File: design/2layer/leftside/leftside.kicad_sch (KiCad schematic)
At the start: 227 parts, among them IC2 MCP23009-E_MG, IC3 nRF52833-QDAA-R7, IC5 XCL110A503KR-G, IC6 TPS22917LDBVT, IC7 SN74AHCT1G125DCKR, IC8 TPS63051RMWT, J1 USB_C_Receptacle_USB2.0_16P, J2 Battery+, J3 Battery-, J4 OLED_128x32, J5 Conn_01x01, J6 Conn_01x04, J7 F32Q-1A7H1-11012, J8 Conn_01x01, U1 BQ27441-G1, U2 BQ24072RGT, U3 USB6B1, U5 PEC11L-4015F-S0015, Y1 ECS-320-8-37B2-JTY-TR

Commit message: Left side pre-stich
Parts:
- removed 3v3_1: TestPoint, TestPoint:TestPoint_Pad_D1.5mm, symbol Connector:TestPoint
- removed Di31, Di32, Di33, Di35: Diode, ScottoKeebs_Components:Diode_SOD-123, symbol ScottoKeebs:Placeholder_Diode
- removed S14, S24, S32, S33, S34, S36, S8: Keyswitch, ScottoKeebs_Hotswap:Hotswap_Choc_V1V2_Plated_1.00u, symbol ScottoKeebs:Placeholder_Keyswitch
- added C2, C3, C4: 100nF, ScottoKeebs_Components:Capacitor_0603, symbol Device:C_Small
- added D49, D50, D51, D52, D53, D54, D55, D56, D57, D58, D59, D60, D61, D62, D63: LED_SK6812MINI, ScottoKeebs_Components:LED_SK6812MINI, symbol ScottoKeebs:LED_SK6812MINI
- added PC3: 10uF, ScottoKeebs_Components:Capacitor_0603, symbol Device:C_Small
- added S3, S4, S5: Keyswitch, ScottoKeebs_Hotswap:Hotswap_Choc_V1V2_Plated_1.00u, symbol ScottoKeebs:Placeholder_Keyswitch
- J2, J3: footprint Connector_Wire:SolderWire-2.5sqmm_1x01_D2.4mm_OD3.6mm -> Connector_Wire:SolderWire-0.75sqmm_1x01_D1.25mm_OD2.3mm
- J5, J8: footprint (none) -> TestPoint:TestPoint_Pad_1.0x1.0mm
- PG1, VBUS_1, VBUS_USB1: footprint TestPoint:TestPoint_Pad_D1.5mm -> TestPoint:TestPoint_Pad_D1.0mm
- renumbered S25 to S0, S27 to S10, S9 to S11, S10 to S12, S11 to S13, S12 to S14, S28 to S15, S15 to S16, S16 to S17, S17 to S18, S18 to S19, S29 to S20, S20 to S21, S21 to S22, S22 to S23, S23 to S24, S30 to S25, S7 to S26, S13 to S27, S19 to S28, S26 to S29, S31 to S30, S35 to S33, S37 to S35, S3 to S6, S4 to S7, S5 to S8, S6 to S9, R10 to SR10
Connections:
- net 5V: now also C2.1, C3.1, C4.1, D49.1 (VDD), D50.1 (VDD), D51.1 (VDD), D52.1 (VDD), D53.1 (VDD), D54.1 (VDD), D55.1 (VDD), D56.1 (VDD), D57.1 (VDD), D58.1 (VDD), D59.1 (VDD), D60.1 (VDD), D61.1 (VDD), D62.1 (VDD), D63.1 (VDD)
- net CCW: now also IC3.14 (P0.15); no longer IC3.15 (P0.17)
- net CHG: now also IC3.6 (P1.09); no longer IC3.4 (P0.04)
- net CW: now also IC3.15 (P0.17); no longer IC3.14 (P0.15)
- net Column 0: now also IC3.33 (P0.28), S11.1, S16.1, S21.1, S26.1, S6.1; no longer IC3.36 (P0.31), S2.1
- net Column 1: now also S12.1, S17.1, S2.1, S22.1, S27.1, S7.1; no longer S11.1, S16.1, S21.1, S26.1, S6.1
- net Column 2: now also IC3.17 (P0.20), S13.1, S18.1, S23.1, S28.1, S33.1, S8.1, S3.1; no longer IC3.34 (P0.29), S12.1, S17.1, S22.1, S27.1, S7.1
- net Column 3: now also IC3.34 (P0.29), S14.1, S19.1, S24.1, S29.1, S9.1, S4.1; no longer IC3.33 (P0.28), S13.1, S18.1, S23.1, S28.1, S33.1, S8.1
- net Column 4: now also IC3.36 (P0.31), S10.1, S15.1, S20.1, S25.1, S30.1, S35.1, S5.1; no longer IC3.32 (P0.02), S14.1, S19.1, S24.1, S29.1, S9.1
- net GND: now also C2.2, C3.2, C4.2, D49.3 (VSS), D50.3 (VSS), D51.3 (VSS), D52.3 (VSS), D53.3 (VSS), D54.3 (VSS), D55.3 (VSS), D56.3 (VSS), D57.3 (VSS), D58.3 (VSS), D59.3 (VSS), D60.3 (VSS), D61.3 (VSS), D62.3 (VSS), D63.3 (VSS), PC3.2
- net GPOUT: now also IC3.4 (P0.04); no longer IC3.5 (P0.05)
- net INTA: now also IC3.32 (P0.02); no longer IC3.23 (P0.10)
- net LED: now also IC3.31 (P0.03); no longer IC3.17 (P0.20)
- net NO: now also IC3.7 (P0.11); no longer IC3.6 (P1.09)
- net NO2: now also IC3.5 (P0.05); no longer IC3.7 (P0.11)
- net Row 0: now also Di1.1 (K), Di12.1 (K), Di16.1 (K), Di24.1 (K), IC2.12 (GP3); no longer Di10.1 (K), Di2.1 (K), Di26.1 (K), Di8.1 (K), Di9.1 (K), IC2.9 (GP0)
- net Row 1: now also Di10.1 (K), Di2.1 (K), Di26.1 (K), Di8.1 (K), Di9.1 (K), IC2.13 (GP4); no longer Di12.1 (K), Di13.1 (K), Di14.1 (K), Di15.1 (K), Di27.1 (K), Di3.1 (K), IC2.10 (GP1)
- net Row 2: now also Di13.1 (K), Di14.1 (K), Di15.1 (K), Di27.1 (K), Di3.1 (K), IC2.14 (GP5); no longer Di16.1 (K), Di17.1 (K), Di18.1 (K), Di19.1 (K), Di28.1 (K), Di5.1 (K), IC2.11 (GP2)
- net Row 3: now also Di18.1 (K), Di19.1 (K), Di28.1 (K), Di5.1 (K), IC2.15 (GP6); no longer Di22.1 (K), Di23.1 (K), Di24.1 (K), Di29.1 (K), Di6.1 (K), IC2.12 (GP3)
- net Row 4: now also Di17.1 (K), Di22.1 (K), Di23.1 (K), Di29.1 (K), Di6.1 (K), IC2.16 (GP7); no longer Di1.1 (K), Di11.1 (K), Di20.1 (K), Di25.1 (K), Di30.1 (K), Di4.1 (K), IC2.13 (GP4)
- net Row 5: now also Di11.1 (K), Di20.1 (K), Di25.1 (K), Di30.1 (K), Di4.1 (K), IC2.10 (GP1); no longer Di34.1 (K), Di36.1 (K), IC2.14 (GP5)
- net at D6.2 (DOUT): now also D5.4 (DIN); no longer D7.4 (DIN)
- net at D6.4 (DIN): now also D7.2 (DOUT); no longer D5.2 (DOUT)
- net at D17.2 (DOUT): now also D16.4 (DIN); no longer D18.4 (DIN)
- net at D17.4 (DIN): now also D18.2 (DOUT); no longer D16.2 (DOUT)
- net at D3.2 (DOUT): now also D2.4 (DIN); no longer D4.4 (DIN)
- net at D3.4 (DIN): now also D4.2 (DOUT); no longer D2.2 (DOUT)
- net at D28.2 (DOUT): now also D27.4 (DIN); no longer D29.4 (DIN)
- net at D28.4 (DIN): now also D29.2 (DOUT); no longer D27.2 (DOUT)
- net at IC5.1 (1/VIN), IC5.3 (3/EN), IC5.7 (7/L1)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: now also PC3.1
- net at D30.4 (DIN): now also D53.2 (DOUT); no longer D29.2 (DOUT)
- net at D15.2 (DOUT): now also D14.4 (DIN); no longer D16.4 (DIN)
- net at D15.4 (DIN): now also D16.2 (DOUT); no longer D14.2 (DOUT)
- net at D41.2 (DOUT): now also D40.4 (DIN); no longer D42.4 (DIN)
- net at D41.4 (DIN): now also D42.2 (DOUT); no longer D40.2 (DOUT)
- net at D37.2 (DOUT): now also D36.4 (DIN); no longer D38.4 (DIN)
- net at D37.4 (DIN): now also D38.2 (DOUT); no longer D36.2 (DOUT)
- net at D45.2 (DOUT): now also D44.4 (DIN); no longer D46.4 (DIN)
- net at D45.4 (DIN): now also D46.2 (DOUT); no longer D44.2 (DOUT)
- net at D30.2 (DOUT): now also D29.4 (DIN); no longer D31.4 (DIN)
- net at D21.2 (DOUT): now also D20.4 (DIN); no longer D22.4 (DIN)
- net at D21.4 (DIN): now also D22.2 (DOUT); no longer D20.2 (DOUT)
- net at Di16.2 (A): now also S4.2
- net at D35.2 (DOUT): now also D34.4 (DIN); no longer D36.4 (DIN)
- net at D35.4 (DIN): now also D36.2 (DOUT); no longer D34.2 (DOUT)
- net at D33.2 (DOUT): now also D32.4 (DIN); no longer D34.4 (DIN)
- net at D39.4 (DIN): now also D40.2 (DOUT); no longer D38.2 (DOUT)
- net at D47.4 (DIN): now also D26.2 (DOUT); no longer D46.2 (DOUT)
- net at D25.2 (DOUT): now also D24.4 (DIN); no longer D26.4 (DIN)
- net at D25.4 (DIN): now also D23.2 (DOUT); no longer D24.2 (DOUT)
- net at D39.2 (DOUT): now also D38.4 (DIN); no longer D40.4 (DIN)
- net at D19.2 (DOUT): now also D52.4 (DIN); no longer D20.4 (DIN)
- net at Di12.2 (A): now also S3.2
- net at D13.2 (DOUT): now also D12.4 (DIN); no longer D14.4 (DIN)
- net at D13.4 (DIN): now also D14.2 (DOUT); no longer D12.2 (DOUT)
- net at D19.4 (DIN): now also D20.2 (DOUT); no longer D18.2 (DOUT)
- net at D1.2 (DOUT): no longer D2.4 (DIN)
- net at SR10.2: now also D49.4 (DIN); no longer D1.4 (DIN)
- net at D48.2 (DOUT): now also D4.4 (DIN)
- net at D48.4 (DIN): now also D5.2 (DOUT); no longer D47.2 (DOUT)
- net at D43.4 (DIN): now also D44.2 (DOUT); no longer D42.2 (DOUT)
- net at Di24.2 (A): now also S5.2
- net at D8.2 (DOUT): now also D10.4 (DIN); no longer D9.4 (DIN)
- net at D8.4 (DIN): now also D9.2 (DOUT); no longer D7.2 (DOUT)
- net at D33.4 (DIN): now also D34.2 (DOUT); no longer D32.2 (DOUT)
- net at D31.2 (DOUT): now also D54.4 (DIN); no longer D32.4 (DIN)
- net at D23.4 (DIN): now also D47.2 (DOUT); no longer D22.2 (DOUT)
- net at Di17.2 (A): now also S21.2; no longer S16.2
- net at Di21.2 (A): now also S16.2; no longer S21.2
- net at D43.2 (DOUT): now also D56.4 (DIN); no longer D44.4 (DIN)
- net at D11.2 (DOUT): now also D7.4 (DIN); no longer D12.4 (DIN)
- net at D10.2 (DOUT): now also D46.4 (DIN); no longer D11.4 (DIN)
- removed net Column 5: IC3.31 (P0.03), S10.1, S15.1, S20.1, S25.1, S30.1, S35.1
- new net: D58.2 (DOUT), D60.4 (DIN)
- new net: D57.2 (DOUT), D58.4 (DIN)
- new net: D18.4 (DIN), D51.2 (DOUT)
- new net: D51.4 (DIN), D52.2 (DOUT)
- new net: D59.4 (DIN), D60.2 (DOUT)
- new net: D62.4 (DIN), D63.2 (DOUT)
- new net: D59.2 (DOUT), D63.4 (DIN)
- new net: D53.4 (DIN), D54.2 (DOUT)
- new net: D42.4 (DIN), D55.2 (DOUT)
- new net: D55.4 (DIN), D56.2 (DOUT)
- new net: D22.4 (DIN), D24.2 (DOUT)
- new net: D49.2 (DOUT), D50.4 (DIN)
- new net: D1.4 (DIN), D2.2 (DOUT)
- new net: D31.4 (DIN), D32.2 (DOUT)
- new net: D61.4 (DIN), D62.2 (DOUT)
- new net: D61.2 (DOUT), D9.4 (DIN)
- new net: D50.2 (DOUT), D57.4 (DIN)
- new net: D11.4 (DIN), D12.2 (DOUT)
- new net: D26.4 (DIN), D27.2 (DOUT)
- new net Row 6: Di34.1 (K), Di36.1 (K), IC2.11 (GP2)
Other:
- moved on the sheet: C21, C28, C29, C30, C31, C32, C33, C34, C35, C36, C38, C39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

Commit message: LS Kicad 10 migration
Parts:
- removed VBUS_USB1: TestPoint, TestPoint:TestPoint_Pad_D1.0mm, symbol Connector:TestPoint
- EVQWGD1: value ~ -> (none)
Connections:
- net GND: now also J1.SH (SHIELD); no longer J1.S1 (SHIELD)
- net at D49.4 (DIN): now also SR10.1; no longer SR10.2
- net at IC7.4 (Y): now also SR10.2; no longer SR10.1
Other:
- moved on the sheet: 3V3_2, 5V_1, 5V_4, C2, C21, C28, C29, C3, C30, C31, C32, C33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

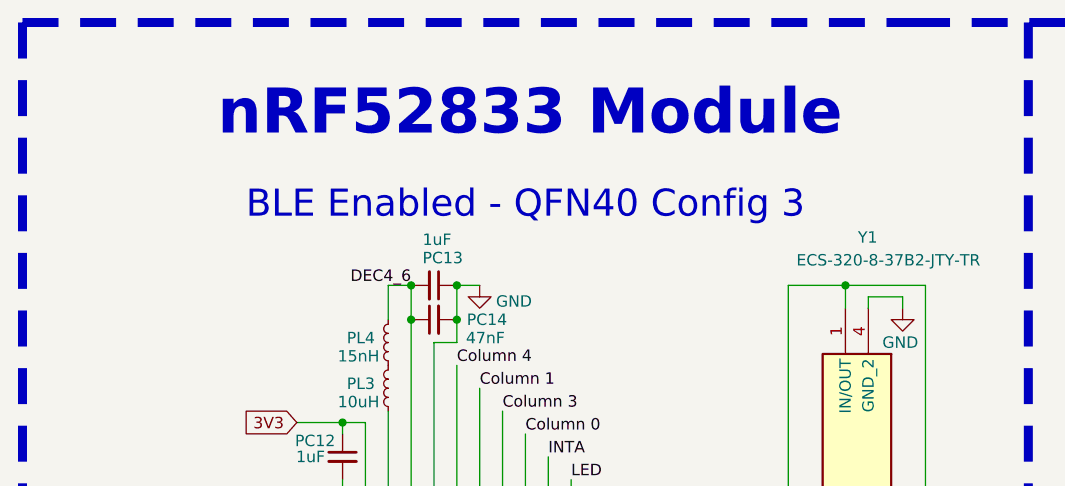
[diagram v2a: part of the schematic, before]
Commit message: RS LED wiring
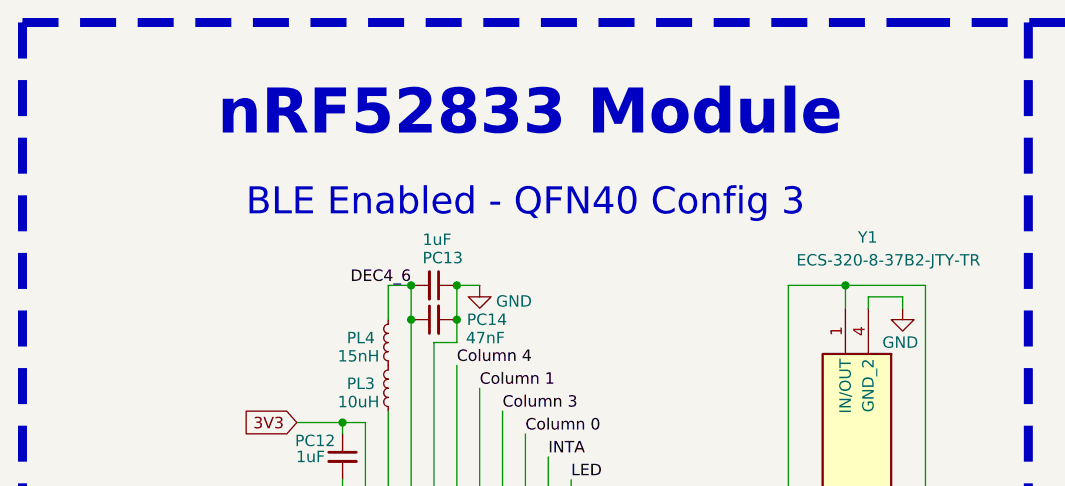
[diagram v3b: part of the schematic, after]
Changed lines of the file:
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@@
 	(text "BLE Enabled - QFN40 Config 3\n"
 		(exclude_from_sim no)
-		(at 69.85 34.29 0)
+		(at 69.85 34.036 0)
 		(effects
 			(font

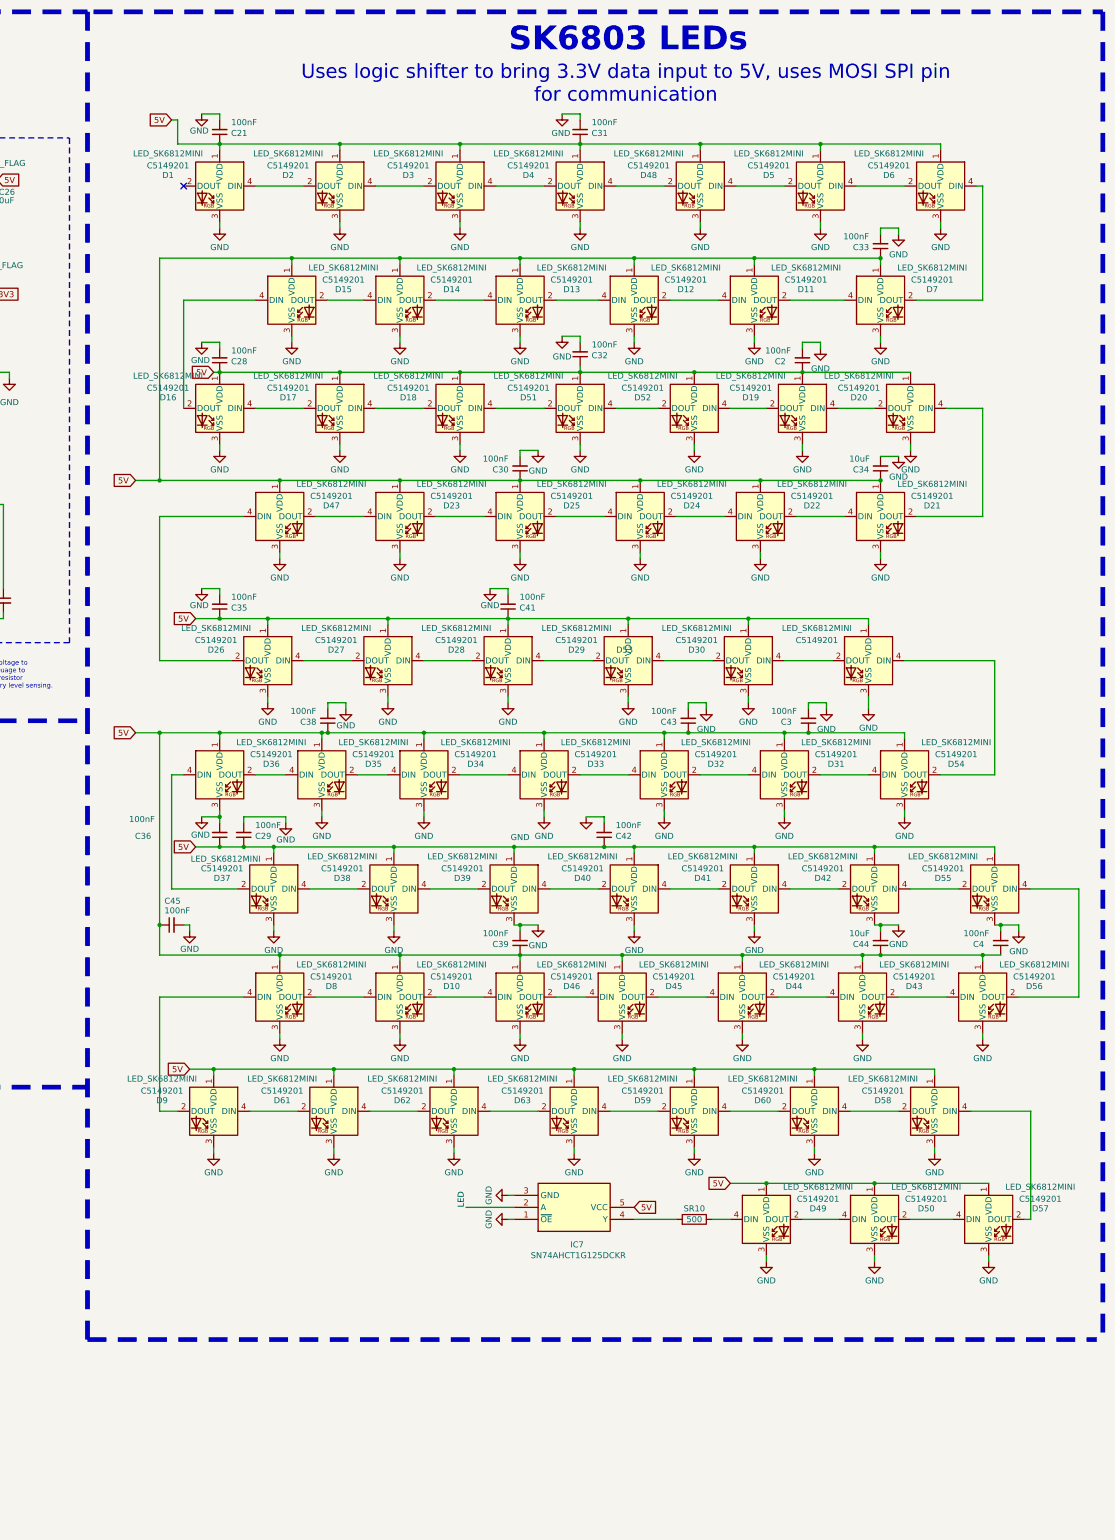
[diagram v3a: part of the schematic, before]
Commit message: Commit before changing via sizes
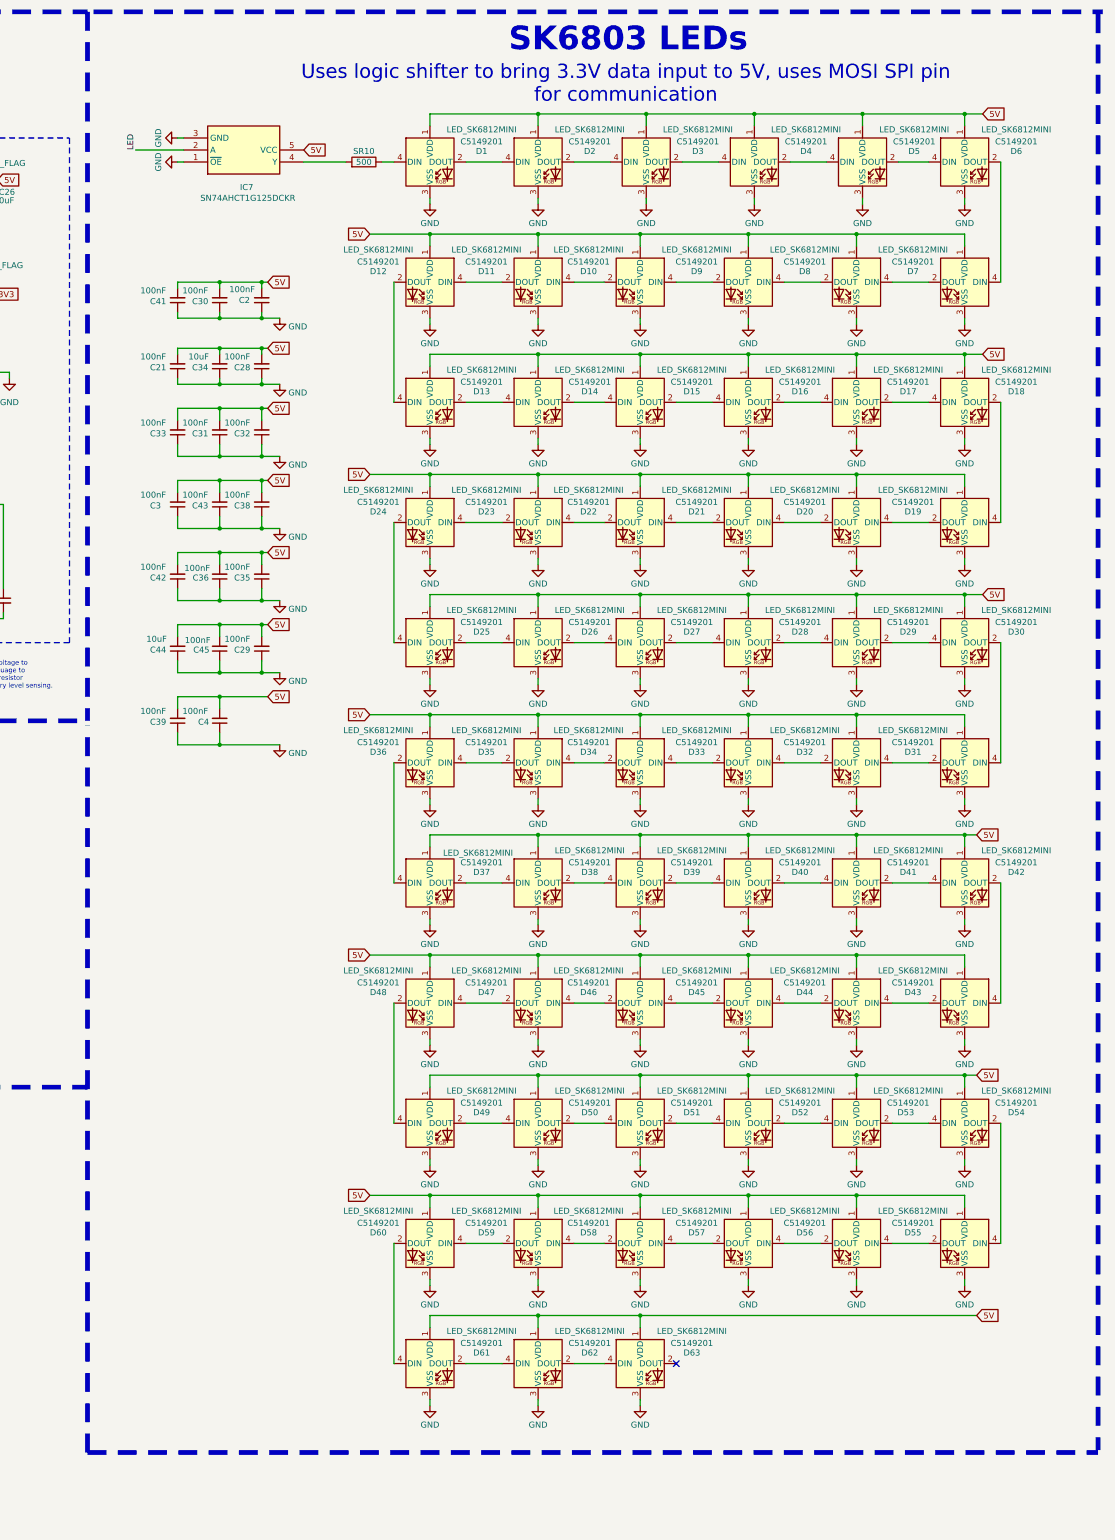
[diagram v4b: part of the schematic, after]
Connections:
- net 5V: now also C2.2, C21.2, C28.2, C29.2, C3.2, C30.2, C31.2, C32.2, C33.2, C34.2, C35.2, C36.2, C38.2, C39.2, C4.2, C41.2, C42.2, C43.2, C44.2, C45.2; no longer C2.1, C21.1, C28.1, C29.1, C3.1, C30.1, C31.1, C32.1, C33.1, C34.1, C35.1, C36.1, C38.1, C39.1, C4.1, C41.1, C42.1, C43.1, C44.1, C45.1
- net GND: now also C2.1, C21.1, C28.1, C29.1, C3.1, C30.1, C31.1, C32.1, C33.1, C34.1, C35.1, C36.1, C38.1, C39.1, C4.1, C41.1, C42.1, C43.1, C44.1, C45.1; no longer C2.2, C21.2, C28.2, C29.2, C3.2, C30.2, C31.2, C32.2, C33.2, C34.2, C35.2, C36.2, C38.2, C39.2, C4.2, C41.2, C42.2, C43.2, C44.2, C45.2
- net at D60.4 (DIN): now also D59.2 (DOUT); no longer D58.2 (DOUT)
- net at D17.2 (DOUT): now also D18.4 (DIN); no longer D16.4 (DIN)
- net at D17.4 (DIN): now also D16.2 (DOUT); no longer D18.2 (DOUT)
- net at D2.4 (DIN): now also D1.2 (DOUT); no longer D3.2 (DOUT)
- net at D3.4 (DIN): now also D2.2 (DOUT); no longer D4.2 (DOUT)
- net at D5.4 (DIN): now also D4.2 (DOUT); no longer D6.2 (DOUT)
- net at D6.4 (DIN): now also D5.2 (DOUT); no longer D7.2 (DOUT)
- net at D28.2 (DOUT): now also D29.4 (DIN); no longer D27.4 (DIN)
- net at D28.4 (DIN): now also D27.2 (DOUT); no longer D29.2 (DOUT)
- net at D30.2 (DOUT): now also D31.4 (DIN); no longer D29.4 (DIN)
- net at D15.2 (DOUT): now also D16.4 (DIN); no longer D14.4 (DIN)
- net at D15.4 (DIN): now also D14.2 (DOUT); no longer D16.2 (DOUT)
- net at D41.2 (DOUT): now also D42.4 (DIN); no longer D40.4 (DIN)
- net at D42.2 (DOUT): now also D43.4 (DIN); no longer D41.4 (DIN)
- net at D51.2 (DOUT): now also D52.4 (DIN); no longer D18.4 (DIN)
- net at D52.2 (DOUT): now also D53.4 (DIN); no longer D51.4 (DIN)
- net at D37.2 (DOUT): now also D38.4 (DIN); no longer D36.4 (DIN)
- net at D37.4 (DIN): now also D36.2 (DOUT); no longer D38.2 (DOUT)
- net at D44.4 (DIN): now also D43.2 (DOUT); no longer D45.2 (DOUT)
- net at D45.4 (DIN): now also D44.2 (DOUT); no longer D46.2 (DOUT)
- net at D53.2 (DOUT): now also D54.4 (DIN); no longer D30.4 (DIN)
- net at D60.2 (DOUT): now also D61.4 (DIN); no longer D59.4 (DIN)
- net at D63.2 (DOUT): no longer D62.4 (DIN)
- net at D63.4 (DIN): now also D62.2 (DOUT); no longer D59.2 (DOUT)
- net at D21.2 (DOUT): now also D22.4 (DIN); no longer D20.4 (DIN)
- net at D21.4 (DIN): now also D20.2 (DOUT); no longer D22.2 (DOUT)
- net at D35.4 (DIN): now also D34.2 (DOUT); no longer D36.2 (DOUT)
- net at D54.2 (DOUT): now also D55.4 (DIN); no longer D53.4 (DIN)
- net at D31.2 (DOUT): now also D32.4 (DIN); no longer D54.4 (DIN)
- net at D33.4 (DIN): now also D32.2 (DOUT); no longer D34.2 (DOUT)
- net at D34.4 (DIN): now also D33.2 (DOUT); no longer D35.2 (DOUT)
- net at D55.2 (DOUT): now also D56.4 (DIN); no longer D42.4 (DIN)
- net at D56.2 (DOUT): now also D57.4 (DIN); no longer D55.4 (DIN)
- net at D39.2 (DOUT): now also D40.4 (DIN); no longer D38.4 (DIN)
- net at D10.2 (DOUT): now also D11.4 (DIN); no longer D46.4 (DIN)
- net at D24.4 (DIN): now also D23.2 (DOUT); no longer D25.2 (DOUT)
- net at D25.4 (DIN): now also D24.2 (DOUT); no longer D23.2 (DOUT)
- net at D39.4 (DIN): now also D38.2 (DOUT); no longer D40.2 (DOUT)
- net at D19.4 (DIN): now also D18.2 (DOUT); no longer D20.2 (DOUT)
- net at D49.4 (DIN): now also D48.2 (DOUT); no longer SR10.1
- net at D12.4 (DIN): now also D11.2 (DOUT); no longer D13.2 (DOUT)
- net at D13.4 (DIN): now also D12.2 (DOUT); no longer D14.2 (DOUT)
- net at D1.4 (DIN): now also SR10.1; no longer D2.2 (DOUT)
- net at D4.4 (DIN): now also D3.2 (DOUT); no longer D48.2 (DOUT)
- net at D48.4 (DIN): now also D47.2 (DOUT); no longer D5.2 (DOUT)
- net at D19.2 (DOUT): now also D20.4 (DIN); no longer D52.4 (DIN)
- net at D10.4 (DIN): now also D9.2 (DOUT); no longer D8.2 (DOUT)
- net at D8.4 (DIN): now also D7.2 (DOUT); no longer D9.2 (DOUT)
- net at D23.4 (DIN): now also D22.2 (DOUT); no longer D47.2 (DOUT)
- net at D47.4 (DIN): now also D46.2 (DOUT); no longer D26.2 (DOUT)
- net at D9.4 (DIN): now also D8.2 (DOUT); no longer D61.2 (DOUT)
- net at D50.2 (DOUT): now also D51.4 (DIN); no longer D57.4 (DIN)
- net at D7.4 (DIN): now also D6.2 (DOUT); no longer D11.2 (DOUT)
- net at D26.4 (DIN): now also D25.2 (DOUT); no longer D27.2 (DOUT)
- new net: D40.2 (DOUT), D41.4 (DIN)
- new net: D29.2 (DOUT), D30.4 (DIN)
- new net: D45.2 (DOUT), D46.4 (DIN)
- new net: D58.2 (DOUT), D59.4 (DIN)
- new net: D13.2 (DOUT), D14.4 (DIN)
- new net: D26.2 (DOUT), D27.4 (DIN)
- new net: D35.2 (DOUT), D36.4 (DIN)
- new net: D61.2 (DOUT), D62.4 (DIN)
